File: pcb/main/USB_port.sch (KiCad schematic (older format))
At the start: 8 parts, among them J4 USB4085-GF-A

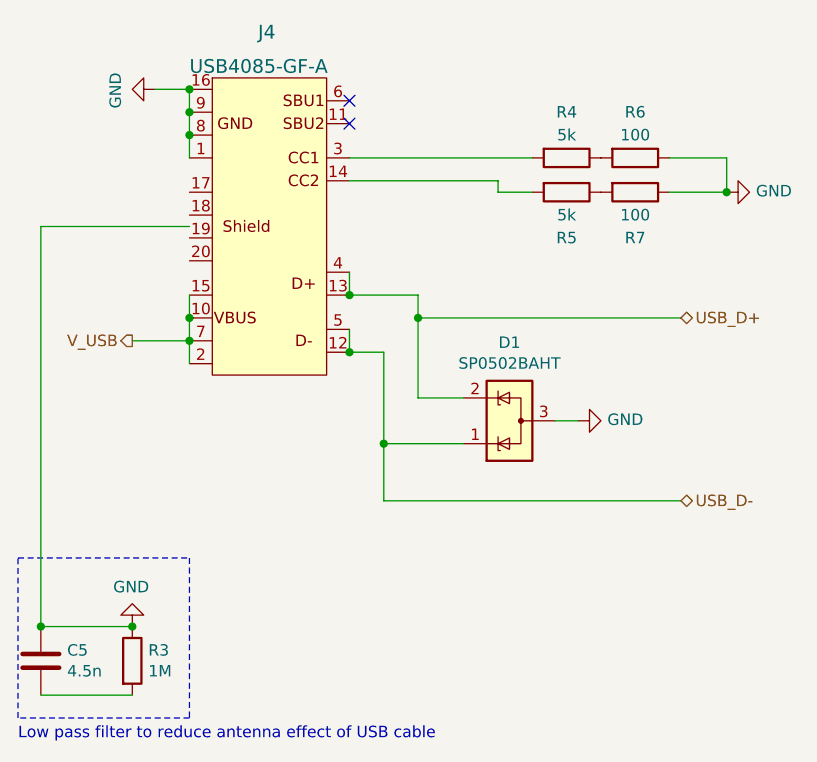
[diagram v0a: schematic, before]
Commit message: Finished PCB layout
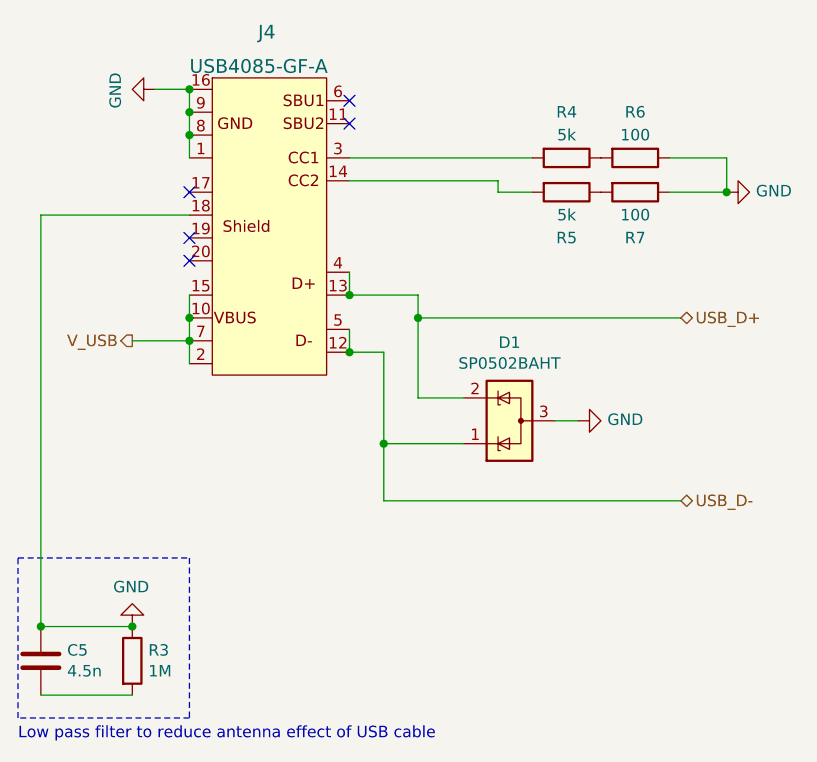
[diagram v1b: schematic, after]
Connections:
- no-connect marks 2 -> 5
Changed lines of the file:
@@
 Text HLabel 4900 3450 0    50   Output ~ 0
 V_USB
-Wire Wire Line
-	5150 2950 4500 2950
-Wire Wire Line
-	4500 2950 4500 4700
 $Comp
 L Device:R R?
@@
 Wire Wire Line
 	4900 3450 5150 3450
+Wire Wire Line
+	5150 2900 4500 2900
+Wire Wire Line
+	4500 2900 4500 4700
+NoConn ~ 5150 2800
+NoConn ~ 5150 3000
+NoConn ~ 5150 3100
 $EndSCHEMATC
